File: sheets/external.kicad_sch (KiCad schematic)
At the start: 3 parts, among them CN3 STE_I2C_QT

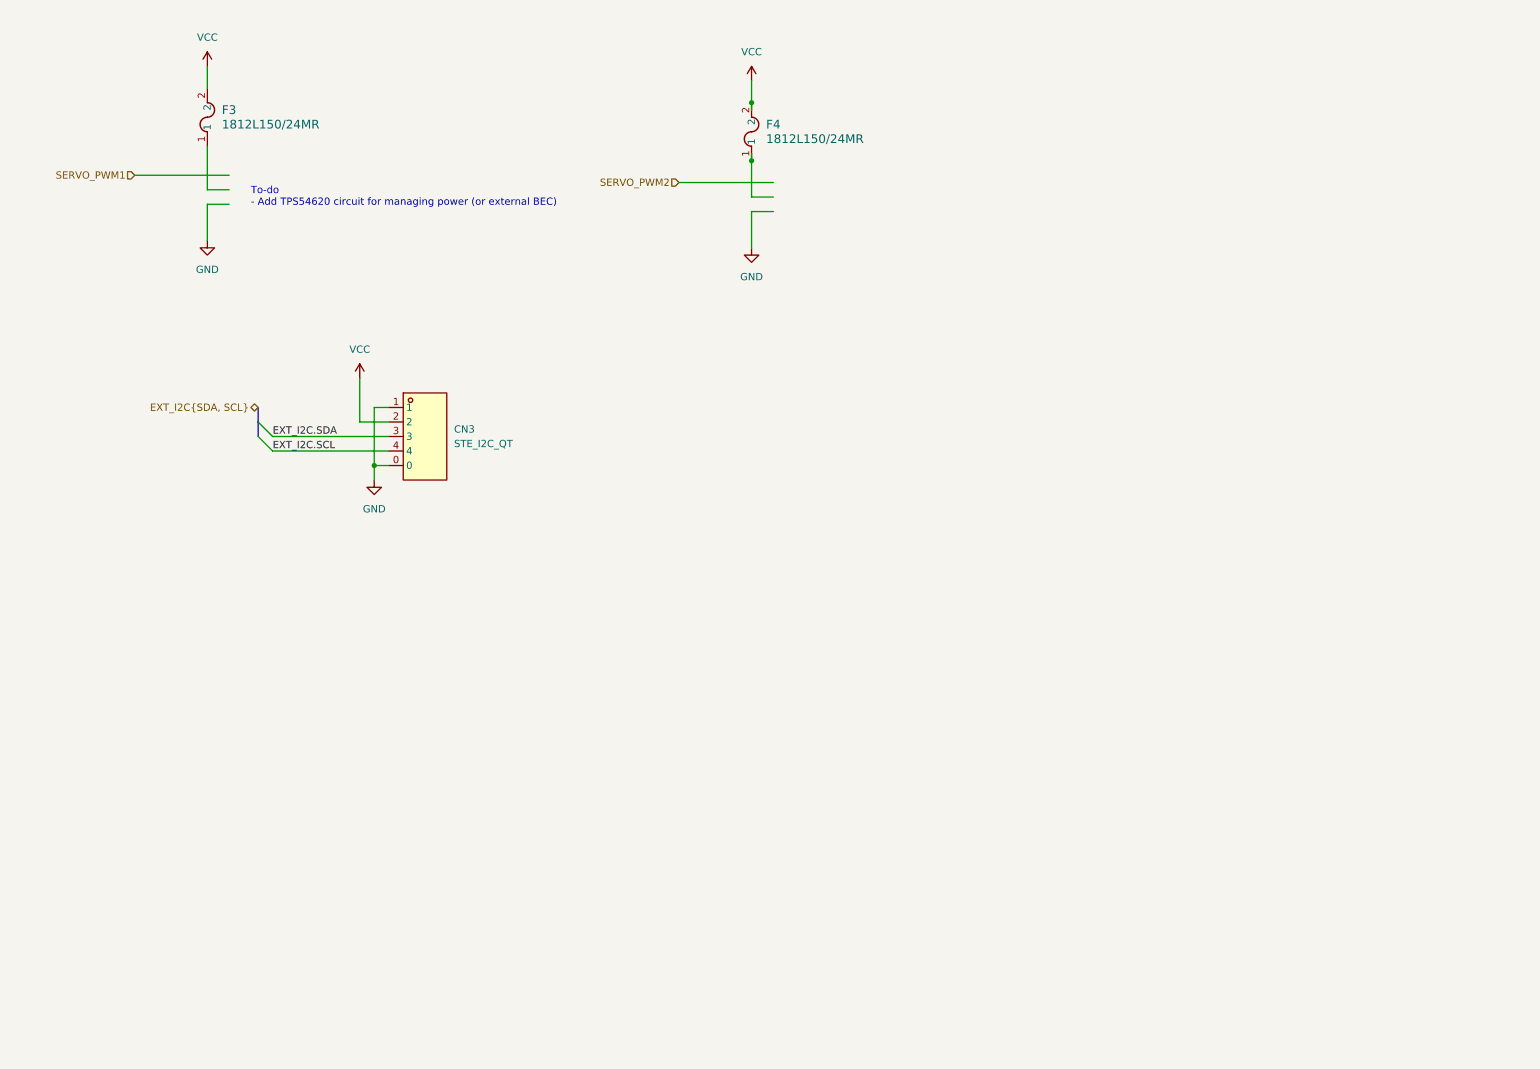
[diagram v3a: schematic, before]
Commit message: polished up circuit, added new 16.8V to 7.4V step down circuit components
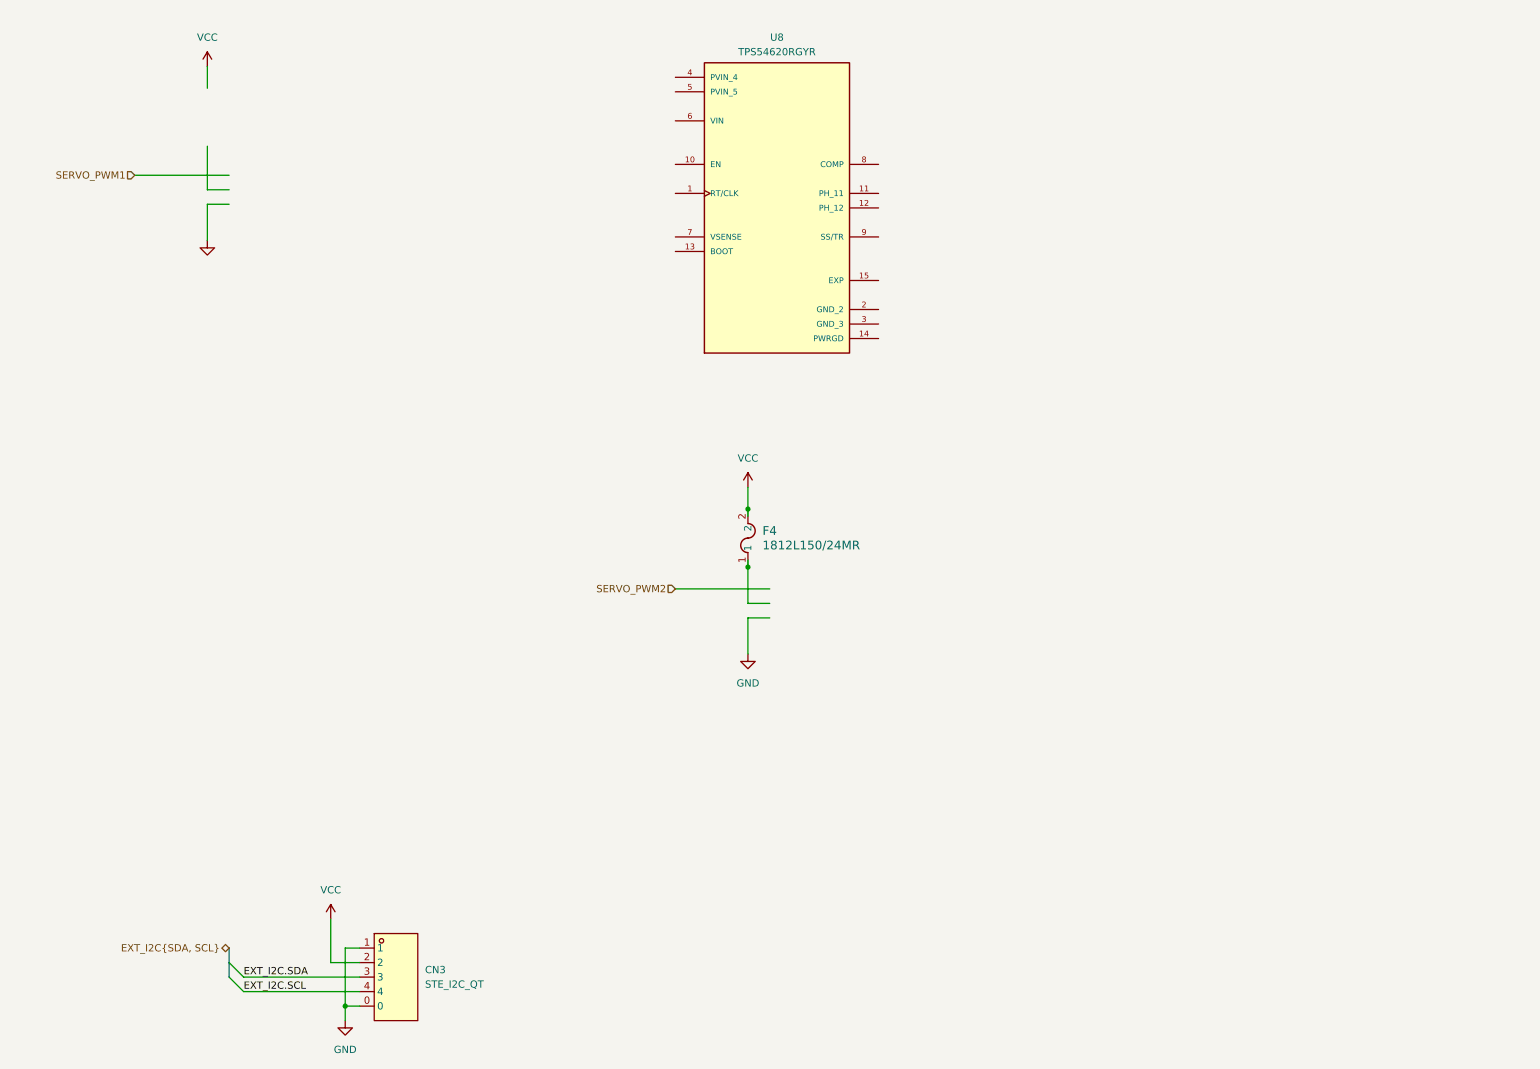
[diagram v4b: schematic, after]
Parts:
- removed F3: 1812L150/24MR, aerolotl_custom:FUSE_1812L150&slash_24_LTF, symbol aerolotl_custom:1812L150_PTC_Fuse
- added U8: TPS54620RGYR, aerolotl_custom:TPS54620_7v4buck, symbol TPS54620RGYR:TPS54620RGYR
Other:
- note removed: "To-do - Add TPS54620 circuit for managing power (or external BEC)"
- moved on the sheet: CN3, F4

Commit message: second push
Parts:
- removed F4: 1812L150/24MR, aerolotl_custom:FUSE_1812L150&slash_24_LTF, symbol aerolotl_custom:1812L150_PTC_Fuse
- removed U8: TPS54620RGYR, aerolotl_custom:TPS54620_7v4buck, symbol TPS54620RGYR:TPS54620RGYR
- added F3, F4: 1812L300/24SLER, aerolotl_custom:F1812, symbol aerolotl_custom:1812L300_24SLER
- added J8, J9: Conn_01x03_Pin, symbol Connector:Conn_01x03_Pin
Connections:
- net GND: now also J8.1 (Pin_1), J9.1 (Pin_1)
- net SERVO_PWM1: now also J8.3 (Pin_3)
- net SERVO_PWM2: now also J9.3 (Pin_3)
- net VCC renamed +3V3
- new net: F3.2, J8.2 (Pin_2)
- new net: F4.2, J9.2 (Pin_2)
- new net +7V4_SERVO: F3.1, F4.1
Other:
- moved on the sheet: CN3

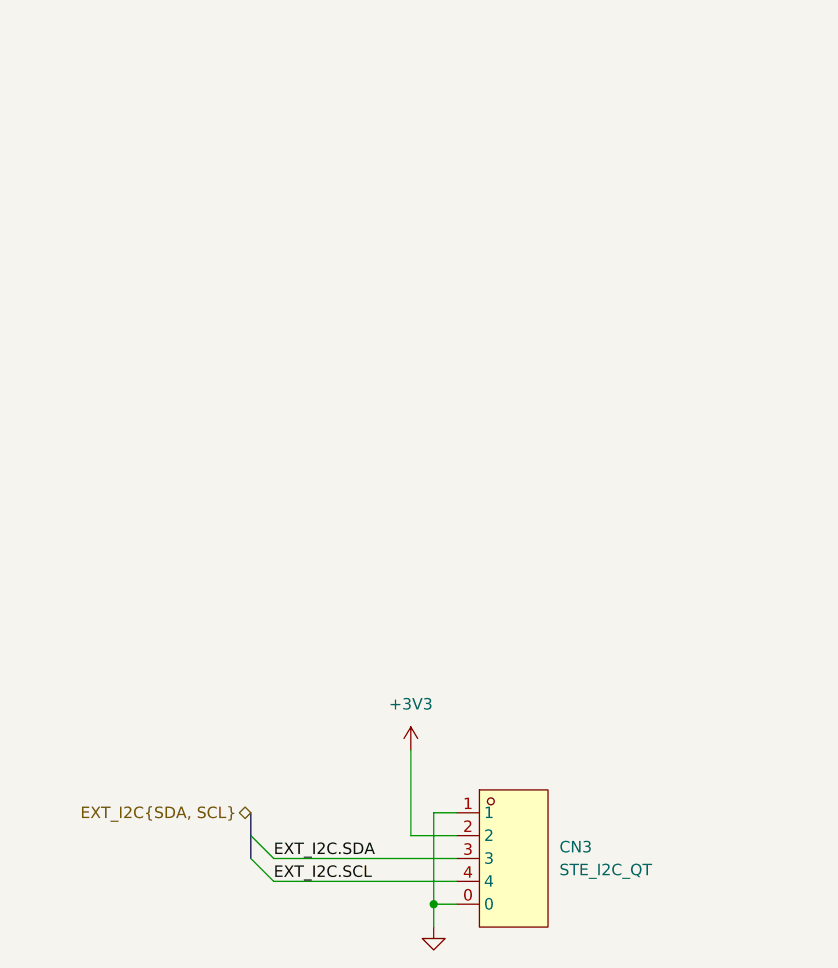
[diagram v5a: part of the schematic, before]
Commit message: Added pinouts for I2C
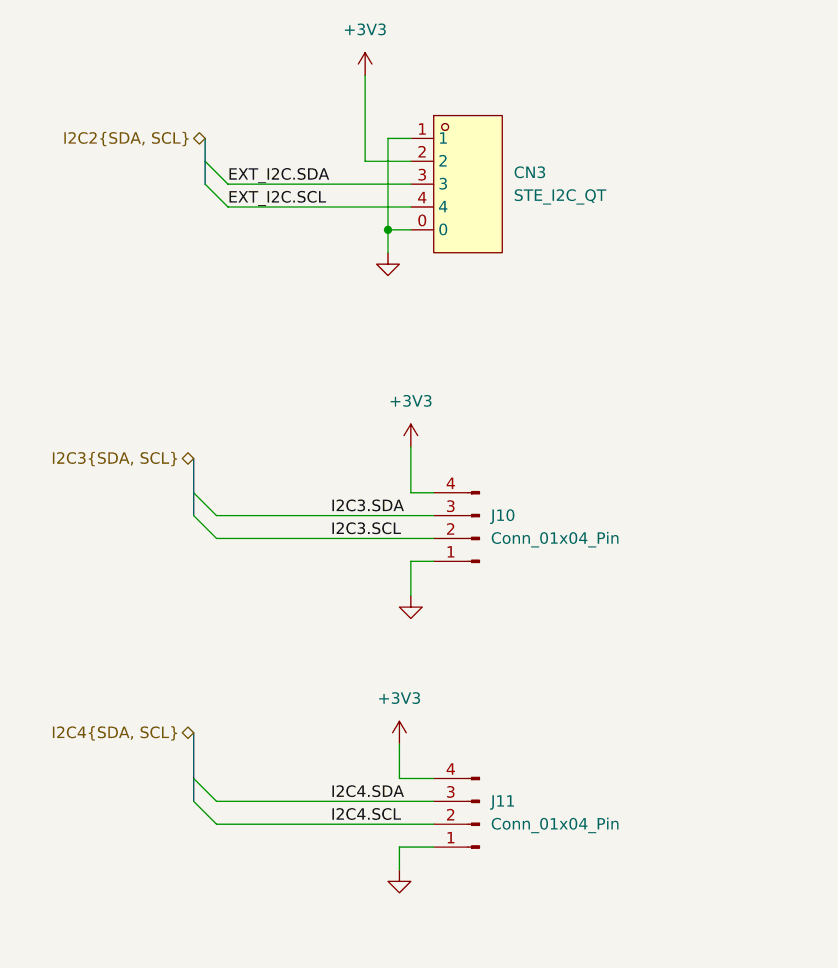
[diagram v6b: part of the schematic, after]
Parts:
- added J10, J11: Conn_01x04_Pin, symbol Connector:Conn_01x04_Pin
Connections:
- net +3V3: now also J10.4 (Pin_4), J11.4 (Pin_4)
- net GND: now also J10.1 (Pin_1), J11.1 (Pin_1)
- new net I2C3.SCL: J10.2 (Pin_2)
- new net I2C3.SDA: J10.3 (Pin_3)
- new net I2C4.SCL: J11.2 (Pin_2)
- new net I2C4.SDA: J11.3 (Pin_3)
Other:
- moved on the sheet: CN3

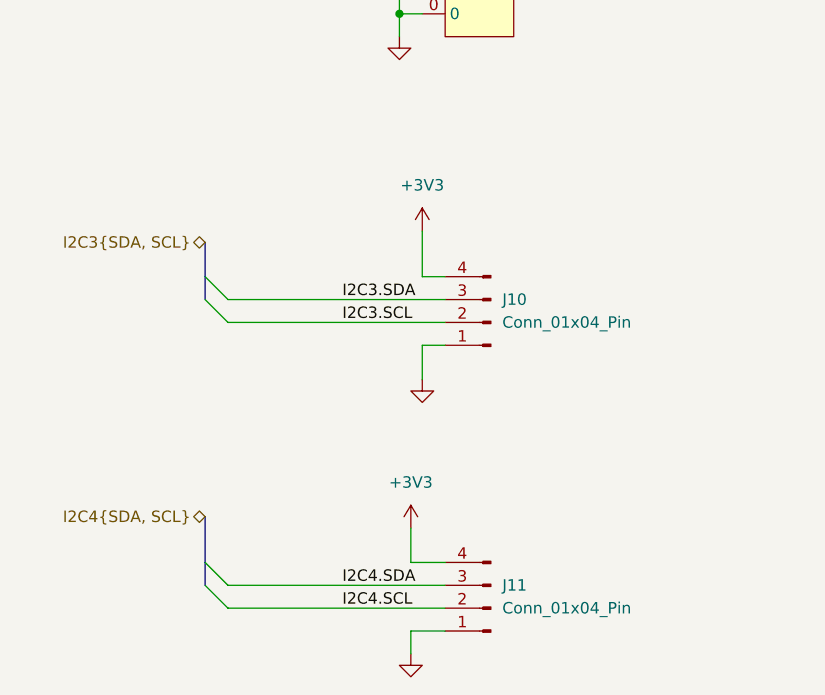
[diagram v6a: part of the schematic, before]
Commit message: Deleted I2C3
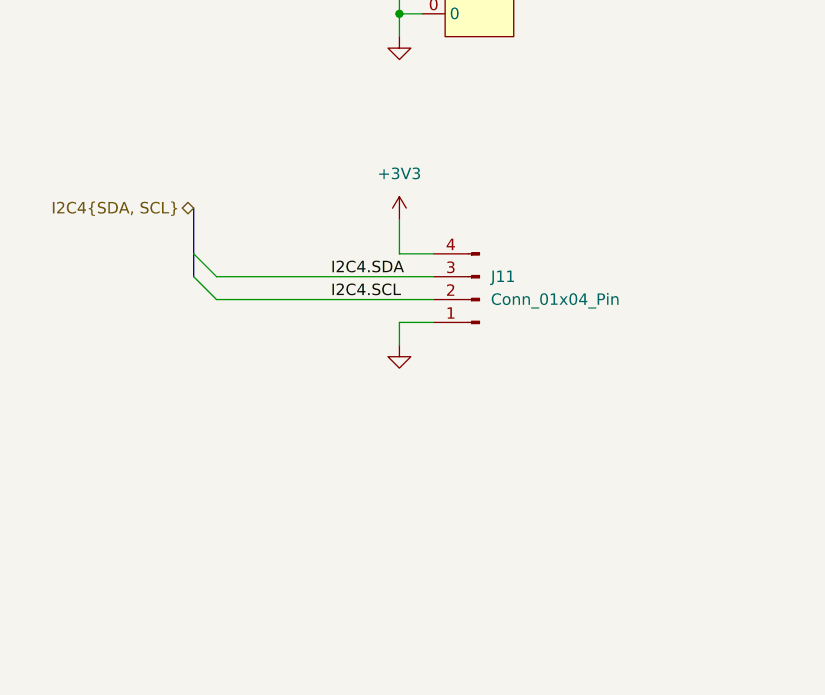
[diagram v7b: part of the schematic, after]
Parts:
- removed J10: Conn_01x04_Pin, symbol Connector:Conn_01x04_Pin
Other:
- moved on the sheet: J11

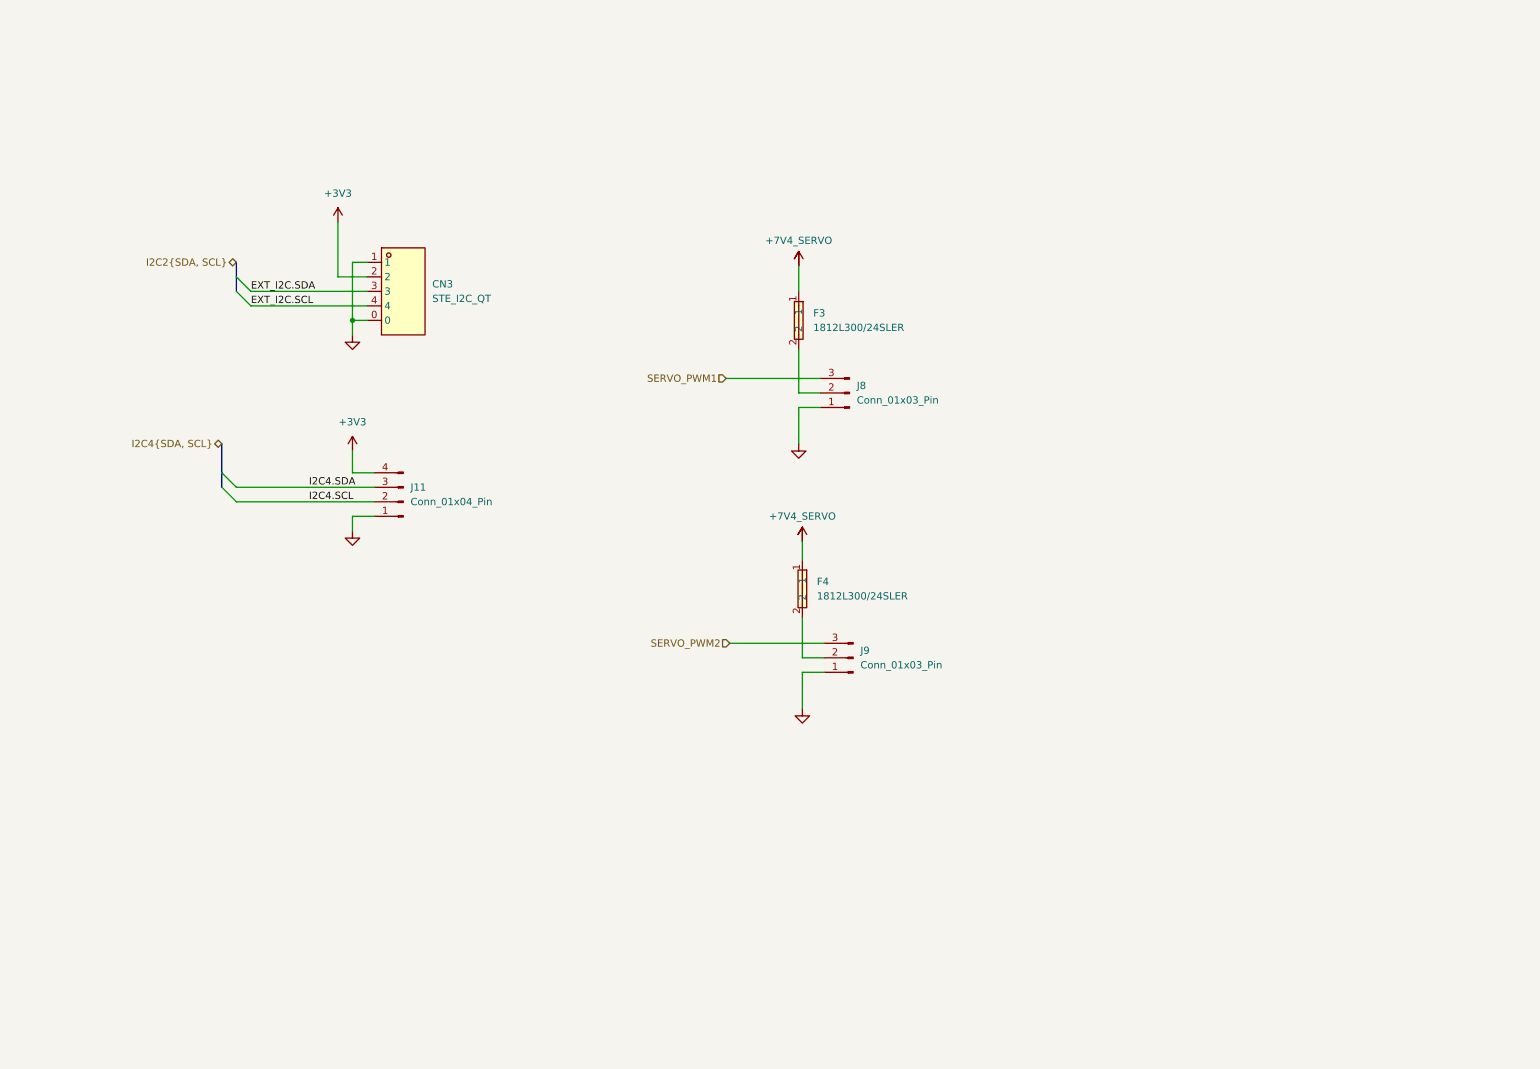
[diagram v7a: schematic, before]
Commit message: removed fd can
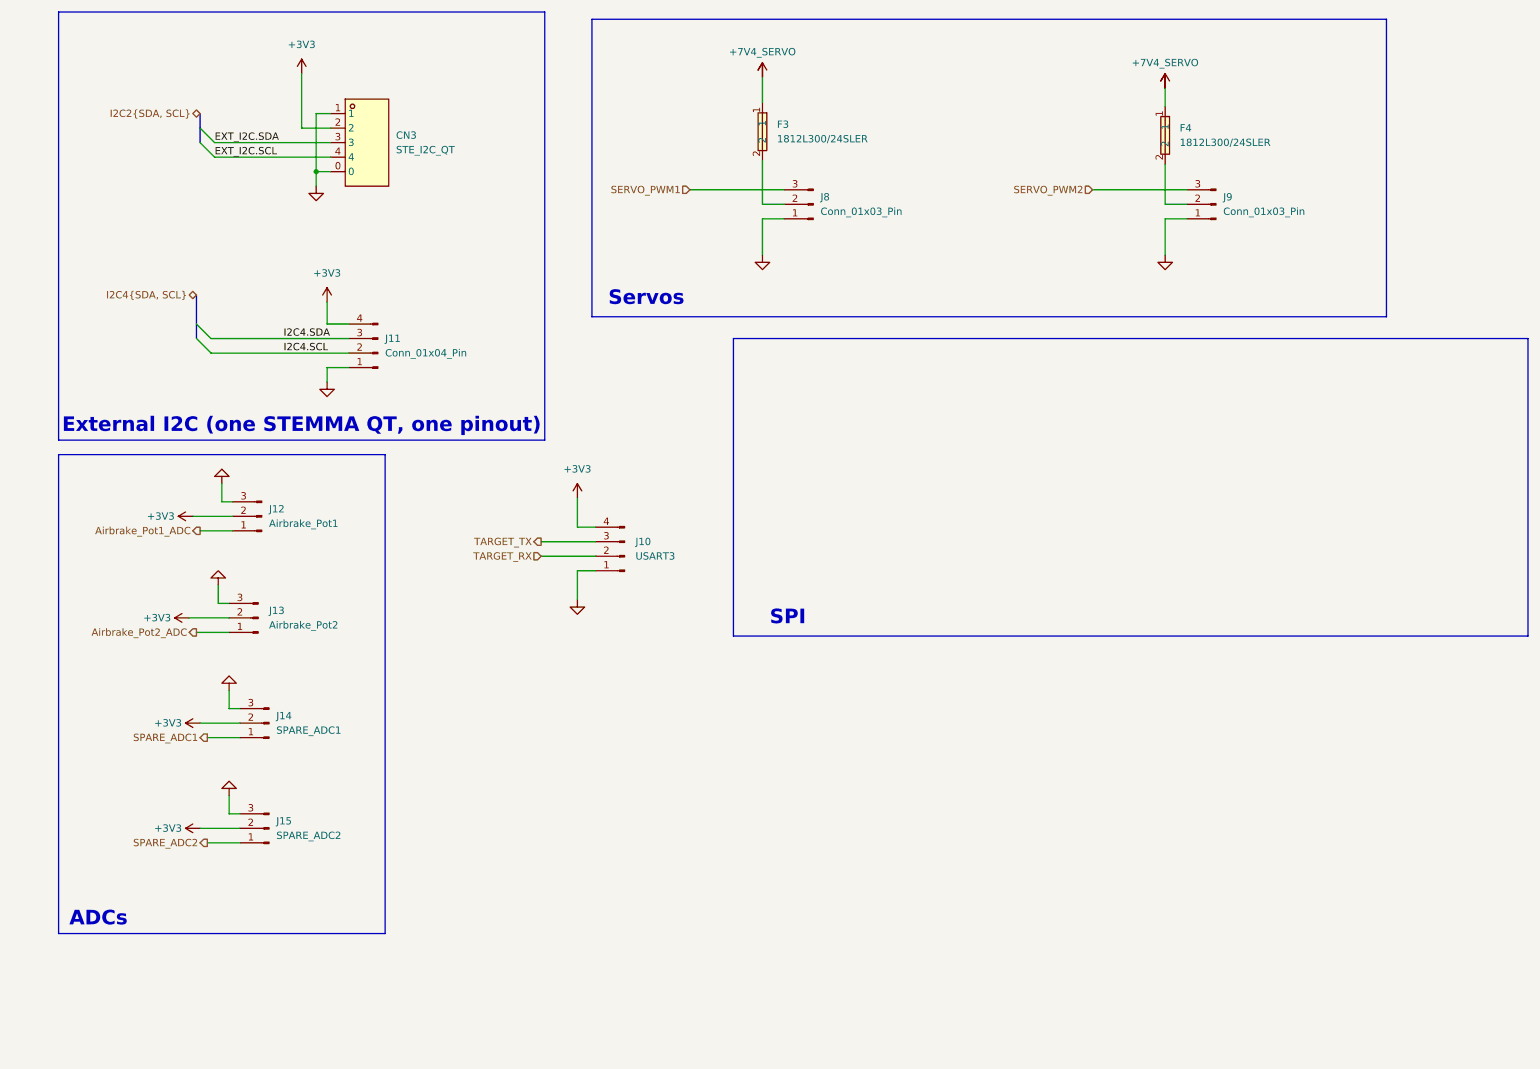
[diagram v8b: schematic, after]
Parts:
- added J10: USART3, symbol Connector:Conn_01x04_Pin
- added J12: Airbrake_Pot1, symbol Connector:Conn_01x03_Pin
- added J13: Airbrake_Pot2, symbol Connector:Conn_01x03_Pin
- added J14: SPARE_ADC1, symbol Connector:Conn_01x03_Pin
- added J15: SPARE_ADC2, symbol Connector:Conn_01x03_Pin
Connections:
- net +3V3: now also J10.4 (Pin_4), J12.2 (Pin_2), J13.2 (Pin_2), J14.2 (Pin_2), J15.2 (Pin_2)
- net GND: now also J10.1 (Pin_1), J12.3 (Pin_3), J13.3 (Pin_3), J14.3 (Pin_3), J15.3 (Pin_3)
- new net Airbrake_Pot1_ADC: J12.1 (Pin_1)
- new net Airbrake_Pot2_ADC: J13.1 (Pin_1)
- new net SPARE_ADC1: J14.1 (Pin_1)
- new net SPARE_ADC2: J15.1 (Pin_1)
- new net TARGET_RX: J10.2 (Pin_2)
- new net TARGET_TX: J10.3 (Pin_3)
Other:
- note added: "ADCs"
- note added: "External I2C (one STEMMA QT, one pinout)"
- note added: "SPI"
- note added: "Servos"
- moved on the sheet: CN3, F3, F4, J11, J8, J9
